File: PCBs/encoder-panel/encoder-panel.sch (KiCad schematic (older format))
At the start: 42 parts, among them J1 Conn_01x05, U1 EN1AJ-B28

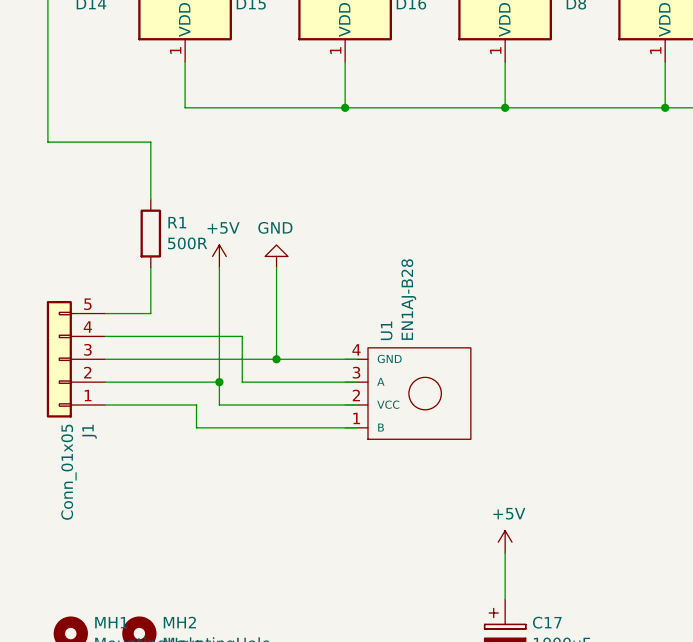
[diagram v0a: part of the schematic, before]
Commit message: updating encoder panel
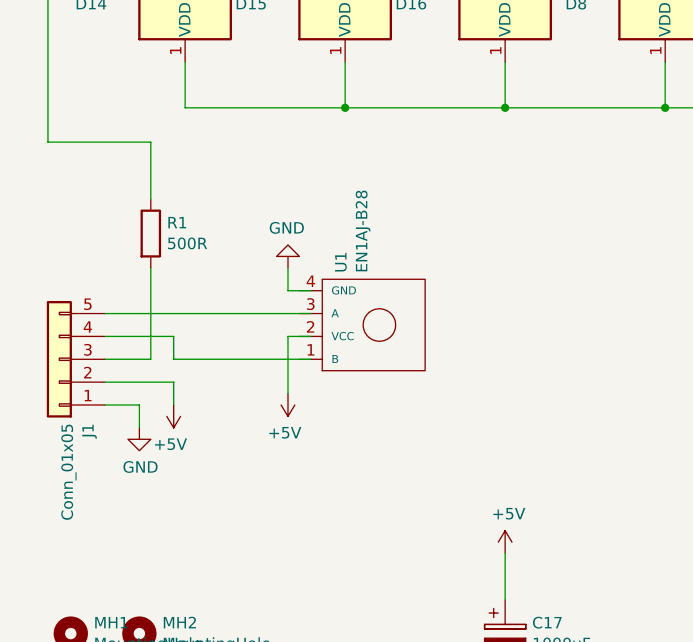
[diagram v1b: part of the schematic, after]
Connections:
- wire segments 163 -> 162
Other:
- moved on the sheet: U1
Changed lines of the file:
@@
 L Bournes-EN-encoder:EN1AJ-B28 U1
 U 1 1 5BB4E9FF
-P 2700 4100
-F 0 "U1" H 2928 4267 50  0000 L CNN
-F 1 "EN1AJ-B28" H 2928 4176 50  0000 L CNN
-F 2 "Bournes-EN:EN1AJ-B28-L100128L-H" H 2700 4100 50  0001 C CNN
-F 3 "" H 2700 4100 50  0001 C CNN
-	1    2700 4100
+P 2500 3800
+F 0 "U1" H 2728 3967 50  0000 L CNN
+F 1 "EN1AJ-B28" H 2728 3876 50  0000 L CNN
+F 2 "Bournes-EN:EN1AJ-B28-L100128L-H" H 2500 3800 50  0001 C CNN
+F 3 "" H 2500 3800 50  0001 C CNN
+	1    2500 3800
 	0    -1   -1   0
 $EndComp
@@
 L power:+5V #PWR04
 U 1 1 5BB907DD
-P 1800 3550
-F 0 "#PWR04" H 1800 3400 50  0001 C CNN
-F 1 "+5V" H 1815 3723 50  0000 C CNN
-F 2 "" H 1800 3550 50  0001 C CNN
-F 3 "" H 1800 3550 50  0001 C CNN
-	1    1800 3550
-	1    0    0    -1
+P 1600 4150
+F 0 "#PWR04" H 1600 4000 50  0001 C CNN
+F 1 "+5V" H 1615 4323 50  0000 C CNN
+F 2 "" H 1600 4150 50  0001 C CNN
+F 3 "" H 1600 4150 50  0001 C CNN
+	1    1600 4150
+	-1   0    0    1
 $EndComp
 $Comp
 L power:GND #PWR05
 U 1 1 5BB90810
-P 2050 3550
-F 0 "#PWR05" H 2050 3300 50  0001 C CNN
-F 1 "GND" H 2055 3377 50  0000 C CNN
-F 2 "" H 2050 3550 50  0001 C CNN
-F 3 "" H 2050 3550 50  0001 C CNN
-	1    2050 3550
-	-1   0    0    1
+P 1450 4250
+F 0 "#PWR05" H 1450 4000 50  0001 C CNN
+F 1 "GND" H 1455 4077 50  0000 C CNN
+F 2 "" H 1450 4250 50  0001 C CNN
+F 3 "" H 1450 4250 50  0001 C CNN
+	1    1450 4250
+	1    0    0    -1
 $EndComp
 $Comp
@@
 Wire Wire Line
 	1050 1450 1050 3000
-Wire Wire Line
-	1500 3550 1500 3750
-Wire Wire Line
-	1500 3750 1300 3750
-Wire Wire Line
-	2050 3550 2050 3950
-Wire Wire Line
-	2050 3950 1300 3950
-Wire Wire Line
-	2400 4250 1700 4250
-Wire Wire Line
-	1700 4250 1700 4150
-Wire Wire Line
-	1700 4150 1300 4150
-Wire Wire Line
-	2400 3950 2050 3950
-Connection ~ 2050 3950
-Wire Wire Line
-	2400 4150 1800 4150
 $Comp
 L Device:C C2
@@
 Wire Wire Line
 	6150 2350 6250 2350
-Wire Wire Line
-	1800 3550 1800 4050
-Wire Wire Line
-	1300 4050 1800 4050
-Connection ~ 1800 4050
-Wire Wire Line
-	1800 4050 1800 4150
-Wire Wire Line
-	2400 4050 1900 4050
-Wire Wire Line
-	1900 4050 1900 3850
-Wire Wire Line
-	1900 3850 1300 3850
 $Comp
 L Mechanical:MountingHole MH3
@@
 Wire Wire Line
 	4450 2850 5150 2850
+Wire Wire Line
+	1300 4150 1450 4150
+Wire Wire Line
+	1450 4150 1450 4250
+Wire Wire Line
+	1300 4050 1600 4050
+Wire Wire Line
+	1600 4050 1600 4150
+Wire Wire Line
+	1300 3950 1500 3950
+Wire Wire Line
+	1500 3550 1500 3950
+$Comp
+L power:GND #PWR?
+U 1 1 5C535563
+P 2100 3550
+F 0 "#PWR?" H 2100 3300 50  0001 C CNN
+F 1 "GND" H 2105 3377 50  0000 C CNN
+F 2 "" H 2100 3550 50  0001 C CNN
+F 3 "" H 2100 3550 50  0001 C CNN
+	1    2100 3550
+	-1   0    0    1
+$EndComp
+$Comp
+L power:+5V #PWR?
+U 1 1 5C5355C2
+P 2100 4100
+F 0 "#PWR?" H 2100 3950 50  0001 C CNN
+F 1 "+5V" H 2115 4273 50  0000 C CNN
+F 2 "" H 2100 4100 50  0001 C CNN
+F 3 "" H 2100 4100 50  0001 C CNN
+	1    2100 4100
+	-1   0    0    1
+$EndComp
+Wire Wire Line
+	2200 3750 1300 3750
+Wire Wire Line
+	2200 3950 1600 3950
+Wire Wire Line
+	1600 3950 1600 3850
+Wire Wire Line
+	1600 3850 1300 3850
+Wire Wire Line
+	2200 3850 2100 3850
+Wire Wire Line
+	2100 3850 2100 4100
+Wire Wire Line
+	2200 3650 2100 3650
+Wire Wire Line
+	2100 3650 2100 3550
 $EndSCHEMATC

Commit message: misc fixes
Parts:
- U1: footprint Bournes-EN:EN1AJ-B28-L100128L-H -> (none)
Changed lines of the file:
@@
-$EndComp
-$Comp
-L Bournes-EN-encoder:EN1AJ-B28 U1
-U 1 1 5BB4E9FF
-P 2500 3800
-F 0 "U1" H 2728 3967 50  0000 L CNN
-F 1 "EN1AJ-B28" H 2728 3876 50  0000 L CNN
-F 2 "Bournes-EN:EN1AJ-B28-L100128L-H" H 2500 3800 50  0001 C CNN
-F 3 "" H 2500 3800 50  0001 C CNN
-	1    2500 3800
-	0    -1   -1   0
 $EndComp
 $Comp
@@
 	1500 3550 1500 3950
 $Comp
-L power:GND #PWR?
+L power:GND #PWR0101
 U 1 1 5C535563
 P 2100 3550
-F 0 "#PWR?" H 2100 3300 50  0001 C CNN
+F 0 "#PWR0101" H 2100 3300 50  0001 C CNN
 F 1 "GND" H 2105 3377 50  0000 C CNN
 F 2 "" H 2100 3550 50  0001 C CNN
@@
 $EndComp
 $Comp
-L power:+5V #PWR?
+L power:+5V #PWR0102
 U 1 1 5C5355C2
 P 2100 4100
-F 0 "#PWR?" H 2100 3950 50  0001 C CNN
+F 0 "#PWR0102" H 2100 3950 50  0001 C CNN
 F 1 "+5V" H 2115 4273 50  0000 C CNN
 F 2 "" H 2100 4100 50  0001 C CNN
@@
 Wire Wire Line
 	2100 3650 2100 3550
+$Comp
+L Bournes-EN-encoder:EN1AJ-B28 U1
+U 1 1 5C55CD50
+P 2550 3800
+F 0 "U1" V 2591 3572 50  0000 R CNN
+F 1 "EN1AJ-B28" V 2500 3572 50  0000 R CNN
+F 2 "" H 2550 3850 50  0001 C CNN
+F 3 "" H 2550 3850 50  0001 C CNN
+	1    2550 3800
+	0    -1   -1   0
+$EndComp
 $EndSCHEMATC

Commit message: renaming symbol to correct name
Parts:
- U1: value EN1AJ-B28 -> ENA1J-B28; symbol Bournes-EN-encoder:EN1AJ-B28 -> Bournes-EN-encoder:ENA1J-B28
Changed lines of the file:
@@
 	2100 3650 2100 3550
 $Comp
-L Bournes-EN-encoder:EN1AJ-B28 U1
+L Bournes-EN-encoder:ENA1J-B28 U1
 U 1 1 5C55CD50
 P 2550 3800
 F 0 "U1" V 2591 3572 50  0000 R CNN
-F 1 "EN1AJ-B28" V 2500 3572 50  0000 R CNN
+F 1 "ENA1J-B28" V 2500 3572 50  0000 R CNN
 F 2 "" H 2550 3850 50  0001 C CNN
 F 3 "" H 2550 3850 50  0001 C CNN

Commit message: removing old libraries
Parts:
- removed U1: ENA1J-B28, symbol Bournes-EN-encoder:ENA1J-B28
- added U1: ENA1J-B28, symbol encoder-panel:ENA1J-B28
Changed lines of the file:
@@
 	2100 3650 2100 3550
 $Comp
-L Bournes-EN-encoder:ENA1J-B28 U1
-U 1 1 5C55CD50
+L encoder-panel:ENA1J-B28 U1
+U 1 1 5C54C484
 P 2550 3800
 F 0 "U1" V 2591 3572 50  0000 R CNN

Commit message: tidying up footprints
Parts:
- U1: footprint (none) -> encoder-panel:ENA1J-B28-L00128L
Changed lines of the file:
@@
 F 0 "U1" V 2591 3572 50  0000 R CNN
 F 1 "ENA1J-B28" V 2500 3572 50  0000 R CNN
-F 2 "" H 2550 3850 50  0001 C CNN
+F 2 "encoder-panel:ENA1J-B28-L00128L" H 2550 3850 50  0001 C CNN
 F 3 "" H 2550 3850 50  0001 C CNN
 	1    2550 3800

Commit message: finishing
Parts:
- added C18: 1000uF, Capacitor_SMD:CP_Elec_8x5.4, symbol Device:CP
- added C19, C20: 1000uF, Capacitor_THT:CP_Radial_D8.0mm_P5.00mm, symbol Device:CP
- added LOGO1, LOGO2: Logo_Open_Hardware_Small, Symbol:OSHW-Logo2_9.8x8mm_SilkScreen, symbol Graphic:Logo_Open_Hardware_Small
- C17: footprint Capacitor_SMD:CP_Elec_10x10.5 -> Capacitor_SMD:CP_Elec_8x5.4
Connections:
- wire segments 162 -> 176
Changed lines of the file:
@@
 F 0 "C17" H 3168 5196 50  0000 L CNN
 F 1 "1000uF" H 3168 5105 50  0000 L CNN
-F 2 "Capacitor_SMD:CP_Elec_10x10.5" H 3088 5000 50  0001 C CNN
+F 2 "Capacitor_SMD:CP_Elec_8x5.4" H 3088 5000 50  0001 C CNN
 F 3 "~" H 3050 5150 50  0001 C CNN
 	1    3050 5150
@@
 Connection ~ 6650 3500
 Wire Wire Line
-	3050 5000 3050 4800
-Wire Wire Line
-	3050 5300 3050 5500
+	3050 5000 3050 4900
+Wire Wire Line
+	3050 5300 3050 5400
 Wire Wire Line
 	1950 1450 2050 1450
@@
 	0    -1   -1   0
 $EndComp
+$Comp
+L Device:CP C18
+U 1 1 5C551B62
+P 3350 5150
+F 0 "C18" H 3468 5196 50  0000 L CNN
+F 1 "1000uF" H 3468 5105 50  0000 L CNN
+F 2 "Capacitor_SMD:CP_Elec_8x5.4" H 3388 5000 50  0001 C CNN
+F 3 "~" H 3350 5150 50  0001 C CNN
+	1    3350 5150
+	1    0    0    -1
+$EndComp
+$Comp
+L Device:CP C19
+U 1 1 5C551BCE
+P 3600 5150
+F 0 "C19" H 3718 5196 50  0000 L CNN
+F 1 "1000uF" H 3718 5105 50  0000 L CNN
+F 2 "Capacitor_THT:CP_Radial_D8.0mm_P5.00mm" H 3638 5000 50  0001 C CNN
+F 3 "~" H 3600 5150 50  0001 C CNN
+	1    3600 5150
+	1    0    0    -1
+$EndComp
+$Comp
+L Device:CP C20
+U 1 1 5C551C39
+P 3850 5150
+F 0 "C20" H 3968 5196 50  0000 L CNN
+F 1 "1000uF" H 3968 5105 50  0000 L CNN
+F 2 "Capacitor_THT:CP_Radial_D8.0mm_P5.00mm" H 3888 5000 50  0001 C CNN
+F 3 "~" H 3850 5150 50  0001 C CNN
+	1    3850 5150
+	1    0    0    -1
+$EndComp
+Wire Wire Line
+	3050 4900 3350 4900
+Wire Wire Line
+	3350 4900 3350 5000
+Connection ~ 3050 4900
+Wire Wire Line
+	3050 4900 3050 4800
+Wire Wire Line
+	3350 4900 3600 4900
+Wire Wire Line
+	3600 4900 3600 5000
+Connection ~ 3350 4900
+Wire Wire Line
+	3600 4900 3850 4900
+Wire Wire Line
+	3850 4900 3850 5000
+Connection ~ 3600 4900
+Wire Wire Line
+	3050 5400 3350 5400
+Wire Wire Line
+	3350 5400 3350 5300
+Connection ~ 3050 5400
+Wire Wire Line
+	3050 5400 3050 5500
+Wire Wire Line
+	3350 5400 3600 5400
+Wire Wire Line
+	3600 5400 3600 5300
+Connection ~ 3350 5400
+Wire Wire Line
+	3600 5400 3850 5400
+Wire Wire Line
+	3850 5400 3850 5300
+Connection ~ 3600 5400
+$Comp
+L Graphic:Logo_Open_Hardware_Small LOGO1
+U 1 1 5C582493
+P 950 7350
+F 0 "LOGO1" H 950 7625 50  0001 C CNN
+F 1 "Logo_Open_Hardware_Small" H 950 7125 50  0001 C CNN
+F 2 "Symbol:OSHW-Logo2_9.8x8mm_SilkScreen" H 950 7350 50  0001 C CNN
+F 3 "~" H 950 7350 50  0001 C CNN
+	1    950  7350
+	1    0    0    -1
+$EndComp
+$Comp
+L Graphic:Logo_Open_Hardware_Small LOGO2
+U 1 1 5C582C6A
+P 1450 7350
+F 0 "LOGO2" H 1450 7625 50  0001 C CNN
+F 1 "Logo_Open_Hardware_Small" H 1450 7125 50  0001 C CNN
+F 2 "Symbol:OSHW-Logo2_9.8x8mm_SilkScreen" H 1450 7350 50  0001 C CNN
+F 3 "~" H 1450 7350 50  0001 C CNN
+	1    1450 7350
+	1    0    0    -1
+$EndComp
 $EndSCHEMATC
